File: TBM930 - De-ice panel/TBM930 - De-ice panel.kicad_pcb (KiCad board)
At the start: 2 copper layers, 190.5 x 101.6 mm, 80 parts, among them J1 SW_AIRFRAME_DE_ICE, J10 AVR-ISP-6, J11 Screw_Terminal_01x02, J2 SW_ICE_LIGHT, J3 SW_PROP_DE_ICE, J4 SW_WIND_SHIELD, J5 SW_PITOT_L_HTR, J6 SW_PITOT_R_HTR, J7 SW_INERT_SEP, J8 Barrel_Jack, J9 USB_B_Micro, SW1 SW_Push, SW2 SW_Push, U1 TLC5917IN, U2 TLC5917IN, U3 ATmega32U4-MU, Y1 Crystal_GND24

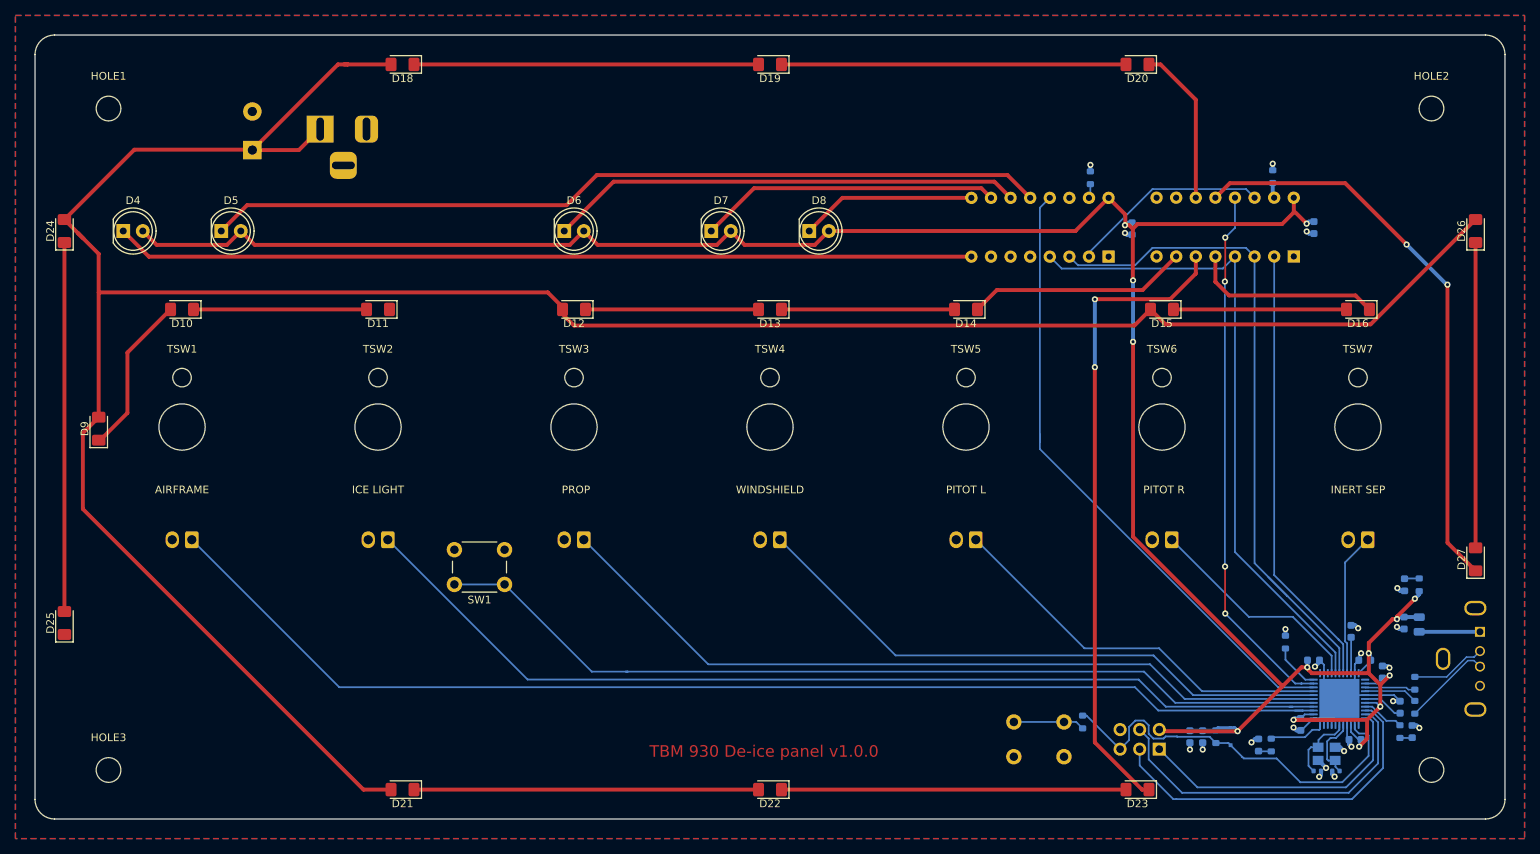
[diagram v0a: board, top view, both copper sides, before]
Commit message: Fully routed v2
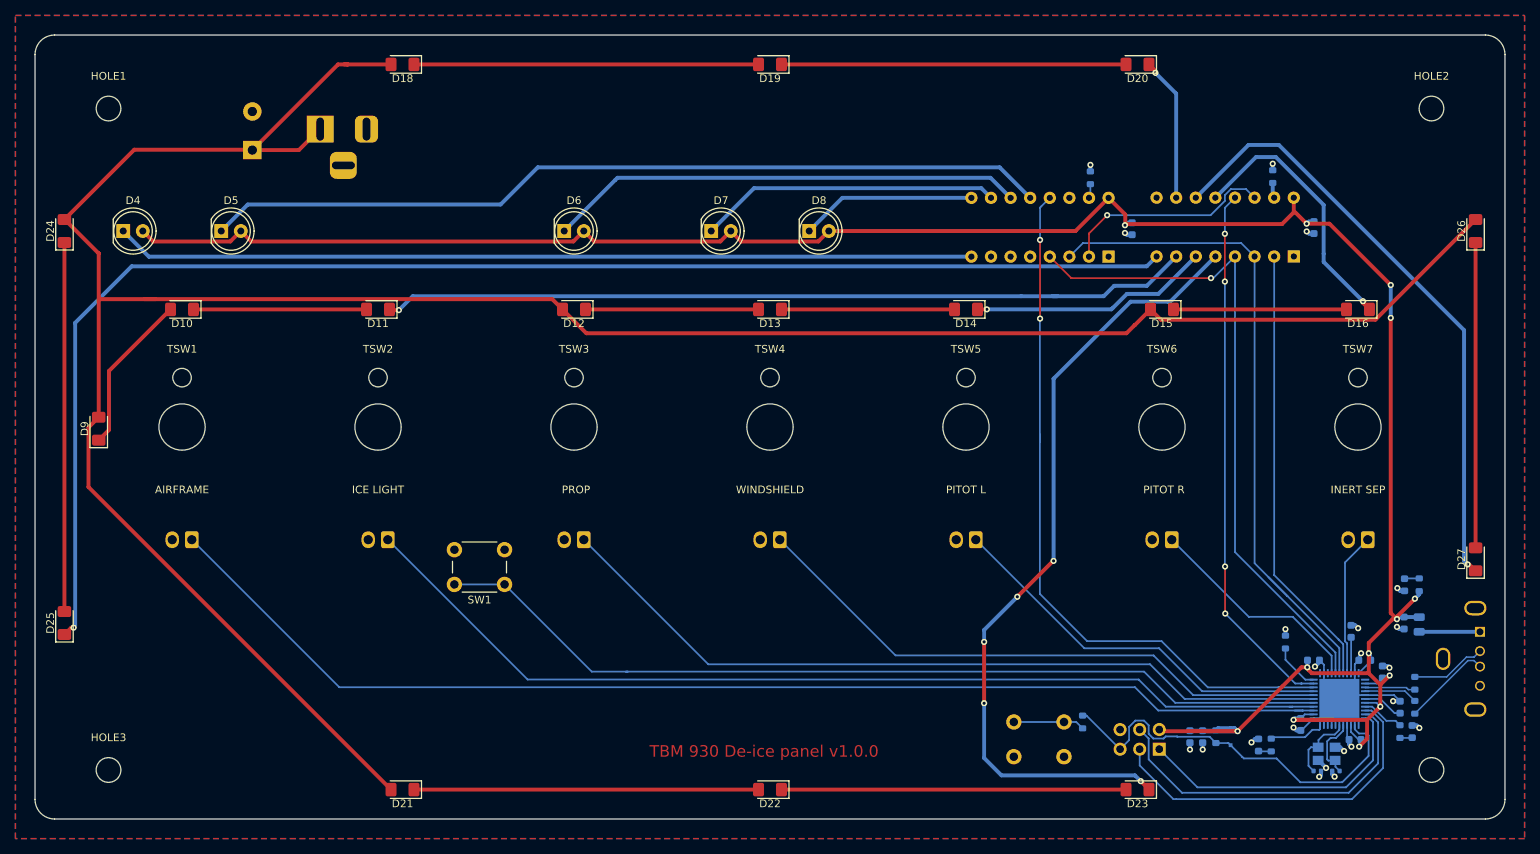
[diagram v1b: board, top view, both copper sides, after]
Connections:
- U1 pad 10: BACKLIGHT6 -> BACKLIGHT4
- U1 pad 11: BACKLIGHT4 -> BACKLIGHT7
- U1 pad 12: BACKLIGHT7 -> BACKLIGHT3
- U1 pad 5: BACKLIGHT3 -> BACKLIGHT5
- U1 pad 6: BACKLIGHT5 -> BACKLIGHT2
- U1 pad 7: BACKLIGHT2 -> BACKLIGHT1
- U1 pad 8: Net-(U1-Pad8) -> BACKLIGHT6
- U1 pad 9: BACKLIGHT1 -> Net-(U1-Pad9)
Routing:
- net BACKLIGHT6: track 0.00 -> 185.5 mm, vias 0 -> 1
- net BACKLIGHT1: track 0.00 -> 105.5 mm, vias 0 -> 1
- net BACKLIGHT5: track 83.6 -> 103.5 mm, vias 2 -> 5
- net INDICATOR_BRIGHT: track 82.3 -> 93.7 mm, vias 0 -> 2
- net +5V: track 339.2 -> 327.8 mm
- net BACKLIGHT3: track 24.7 -> 34.8 mm, vias 0 -> 1
- net BACKLIGHT7: track 74.9 -> 79.5 mm, vias 2 -> 1
- net +12V_LED: track 345.8 -> 343.1 mm
- net BACKLIGHT2: track 28.6 -> 31.3 mm, vias 0 -> 1
- net BACKLIGHT4: track 20.7 -> 18.7 mm, vias 0 -> 1
- net Net-(U1-Pad14): track 25.9 -> 27.8 mm, vias 0 -> 1
- net LED_LATCH: track 84.7 -> 85.7 mm, vias 0 -> 1
- net AIRFRAME_2: track 109.1 -> 109.9 mm

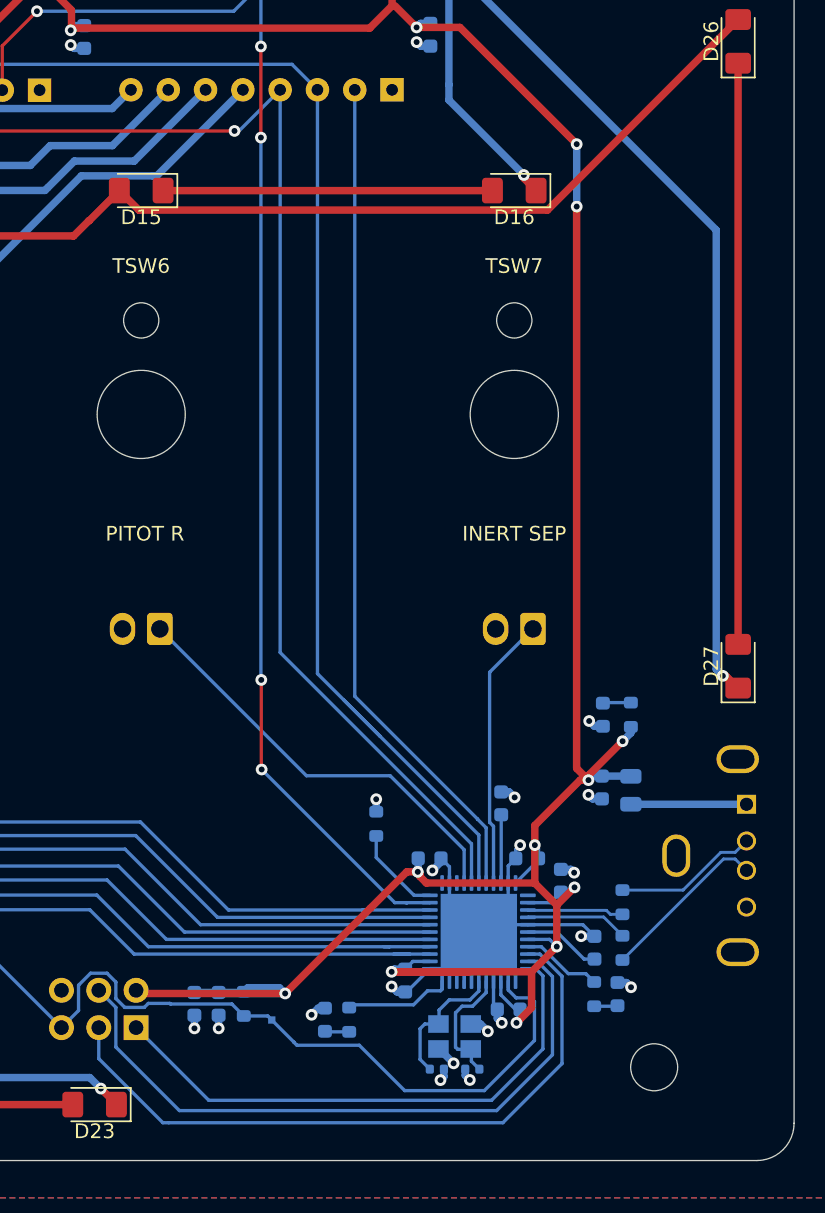
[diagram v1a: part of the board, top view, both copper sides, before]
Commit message: Switch to TQFP
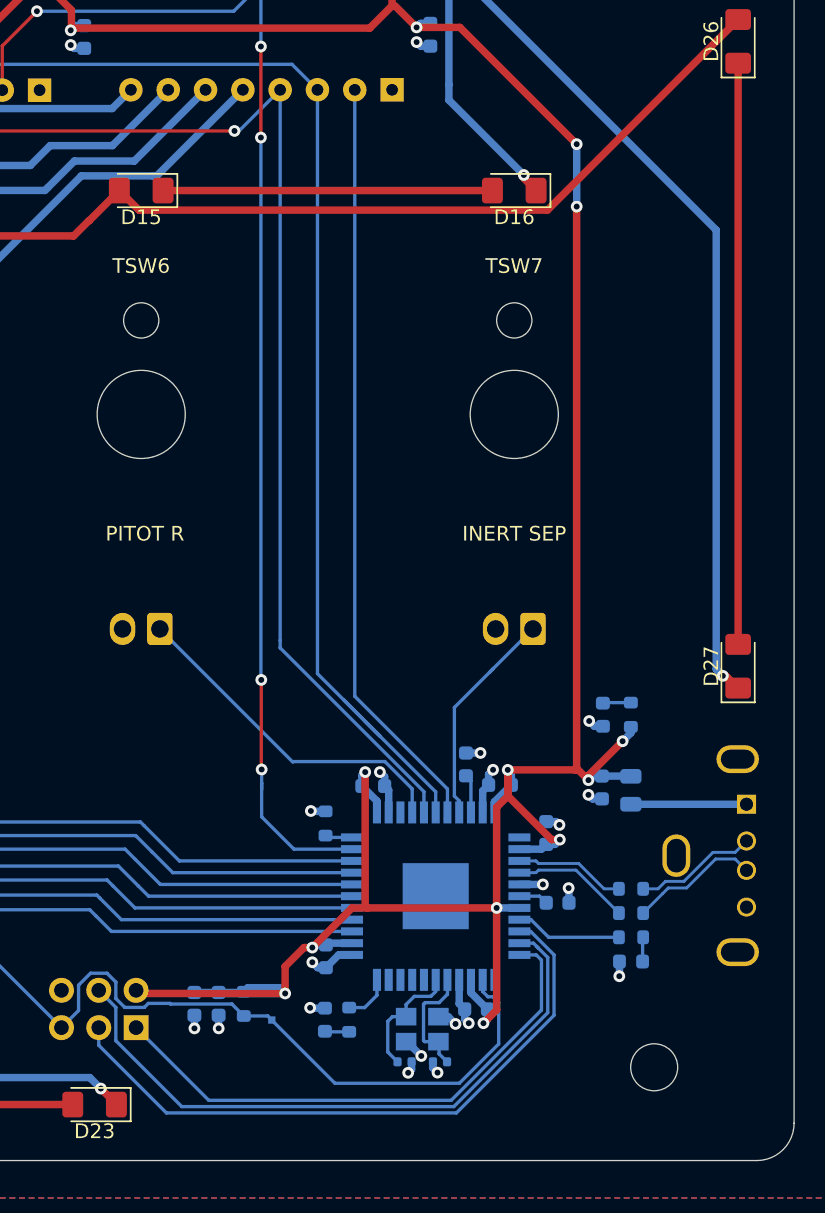
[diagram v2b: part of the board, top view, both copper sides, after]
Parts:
- U3: footprint Package_DFN_QFN:QFN-44-1EP_7x7mm_P0.5mm_EP5.2x5.2mm -> Package_QFP:TQFP-44-1EP_10x10mm_P0.8mm_EP4.5x4.5mm
- moved C2 6.24 mm to (201.2, 118.6)
- moved C5 5.65 mm to (198.0, 130.2)
- moved C4 5.33 mm to (209.8, 118.6)
- moved R2 4.61 mm to (218.8, 128.9), turned to 0 degrees
- moved C7 3.96 mm to (213.8, 126.6), turned to 0 degrees
- moved U3 3.82 mm to (205.5, 126.1)
- moved C6 3.58 mm to (207.5, 117.2)
- moved R11 3.45 mm to (198.0, 121.2)
- moved C1 3.40 mm to (213.0, 121.8)
- moved R7 2.44 mm to (218.8, 127.3), turned to 180 degrees
- moved D1 2.40 mm to (218.8, 130.6), turned to 0 degrees
- moved C17 2.26 mm to (205.8, 137.4)
- moved C16 2.26 mm to (203.3, 137.4)
- moved Y1 2.26 mm to (204.6, 135.2)
- moved C3 2.22 mm to (208.2, 133.8)
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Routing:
- net GND: track 55.5 -> 32.6 mm, vias 22 -> 23
- net INDICATOR_BRIGHT: track 93.7 -> 86.6 mm
- net SW_AIRFRAME: track 155.6 -> 148.6 mm
- net SW_PITOT_L: track 51.9 -> 45.4 mm
- net SW_ICE_LIGHT: track 129.3 -> 122.9 mm
- net SW_WINDSHIELD: track 77.5 -> 71.1 mm
- net SW_PROP: track 103.1 -> 96.8 mm
- net SW_LTS_TEST: track 118.0 -> 111.8 mm
- net LED_LATCH: track 85.7 -> 79.6 mm
- net SW_PITOT_R: track 29.2 -> 23.3 mm
- net LED_DATA: track 57.7 -> 52.6 mm
- net BACKLIGHT_BRIGHT: track 69.9 -> 65.2 mm
- net LED_CLOCK: track 87.5 -> 82.9 mm
- net Net-(R11-Pad1): track 6.18 -> 1.85 mm
- net Net-(R5-Pad2): track 7.40 -> 3.56 mm
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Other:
- net class GND added: clearance 0.2, trace_width 0.508, via_dia 0.8, via_drill 0.4
- net class POWER: trace_width 0.2286 -> 0.508

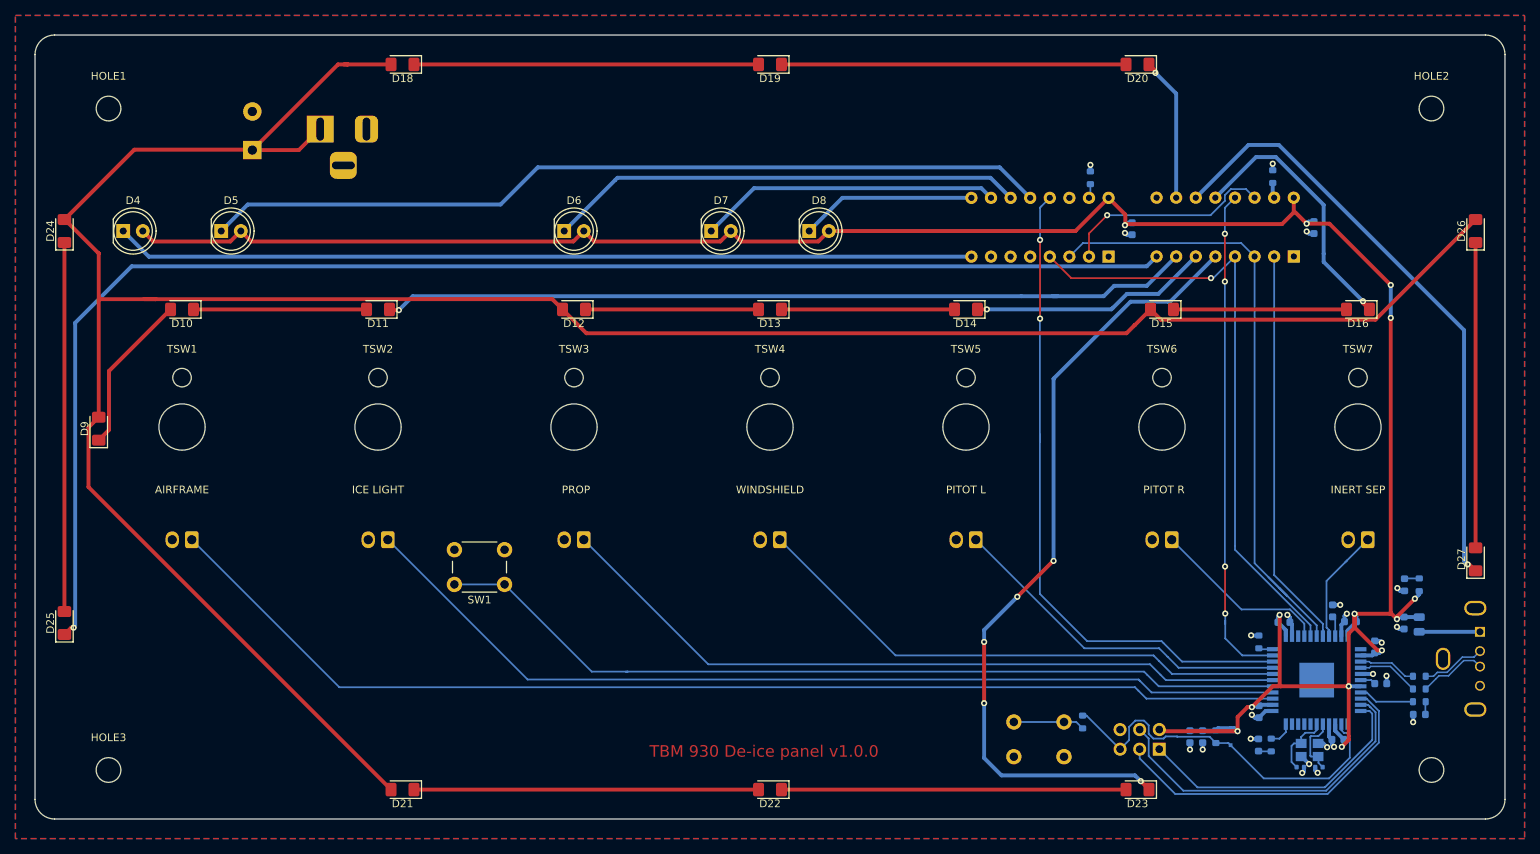
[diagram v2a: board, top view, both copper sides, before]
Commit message: Lots of minor updates to silk screen and vias
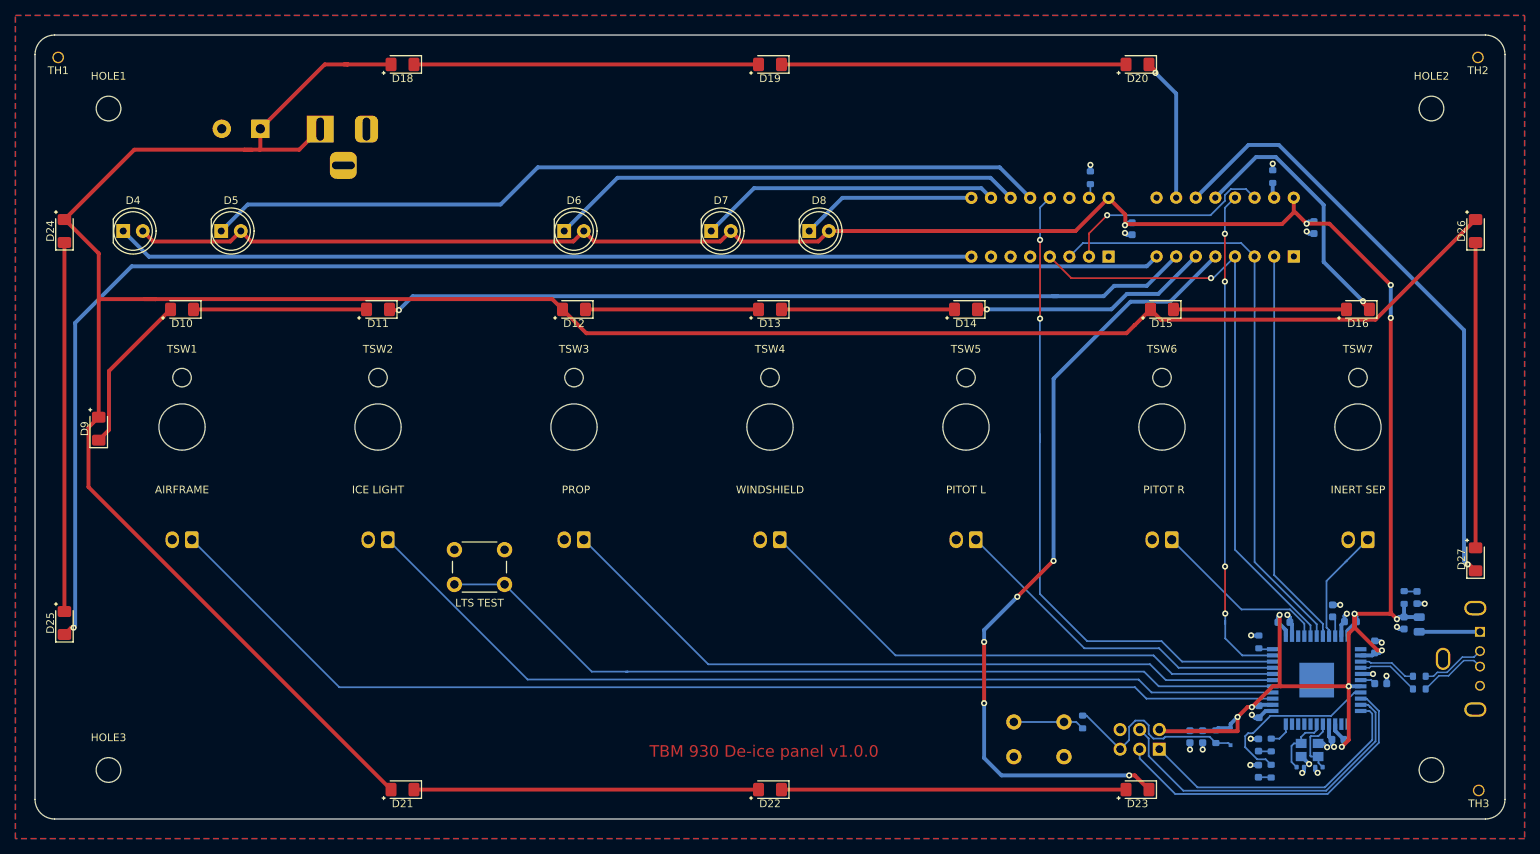
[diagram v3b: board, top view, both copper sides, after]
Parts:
- added TH1: JLCPCB_Tooling_Hole, Global MobiFlight panel parts:JLCPCB_Tooling_Hole, F.Cu at (42.4, 45.5)
- added TH2: JLCPCB_Tooling_Hole, Global MobiFlight panel parts:JLCPCB_Tooling_Hole, F.Cu at (226.4, 45.5)
- added TH3: JLCPCB_Tooling_Hole, Global MobiFlight panel parts:JLCPCB_Tooling_Hole, F.Cu at (226.5, 140.5)
- D1, D2, D3: footprint LED_SMD:LED_0603_1608Metric -> Global MobiFlight panel parts:LED_0603_1608Metric
- D10, D11, D12, D13, D14, D15, D16, D18, D19, D20, D21, D22, D23, D24, D25, D26, D27, D9: footprint LED_SMD:LED_1206_3216Metric_Pad1.42x1.75mm_HandSolder -> Global MobiFlight panel parts:LED_1206_3216Metric_Pad1.42x1.75mm_HandSolder
- LTS TEST: renamed from SW1
- moved D1 22.1 mm to (197.9, 137.9), turned to 270 degrees
- moved R2 21.2 mm to (199.6, 137.9), turned to 270 degrees
- moved J11 2.95 mm to (68.6, 54.7), turned to 180 degrees
- moved R6 2.55 mm to (216.8, 115.4)
- moved D3 2.31 mm to (218.5, 115.4)
- renumbered SW2 to RESET
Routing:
- net RESET: track 49.1 -> 25.7 mm
- net /D17: track 7.27 -> 23.1 mm
- net +5V: track 325.9 -> 319.1 mm, vias 13 -> 12
- net LED_CLOCK: track 82.9 -> 78.0 mm
- net +12V_LED: track 343.1 -> 344.1 mm
